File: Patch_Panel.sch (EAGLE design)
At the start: 24 parts

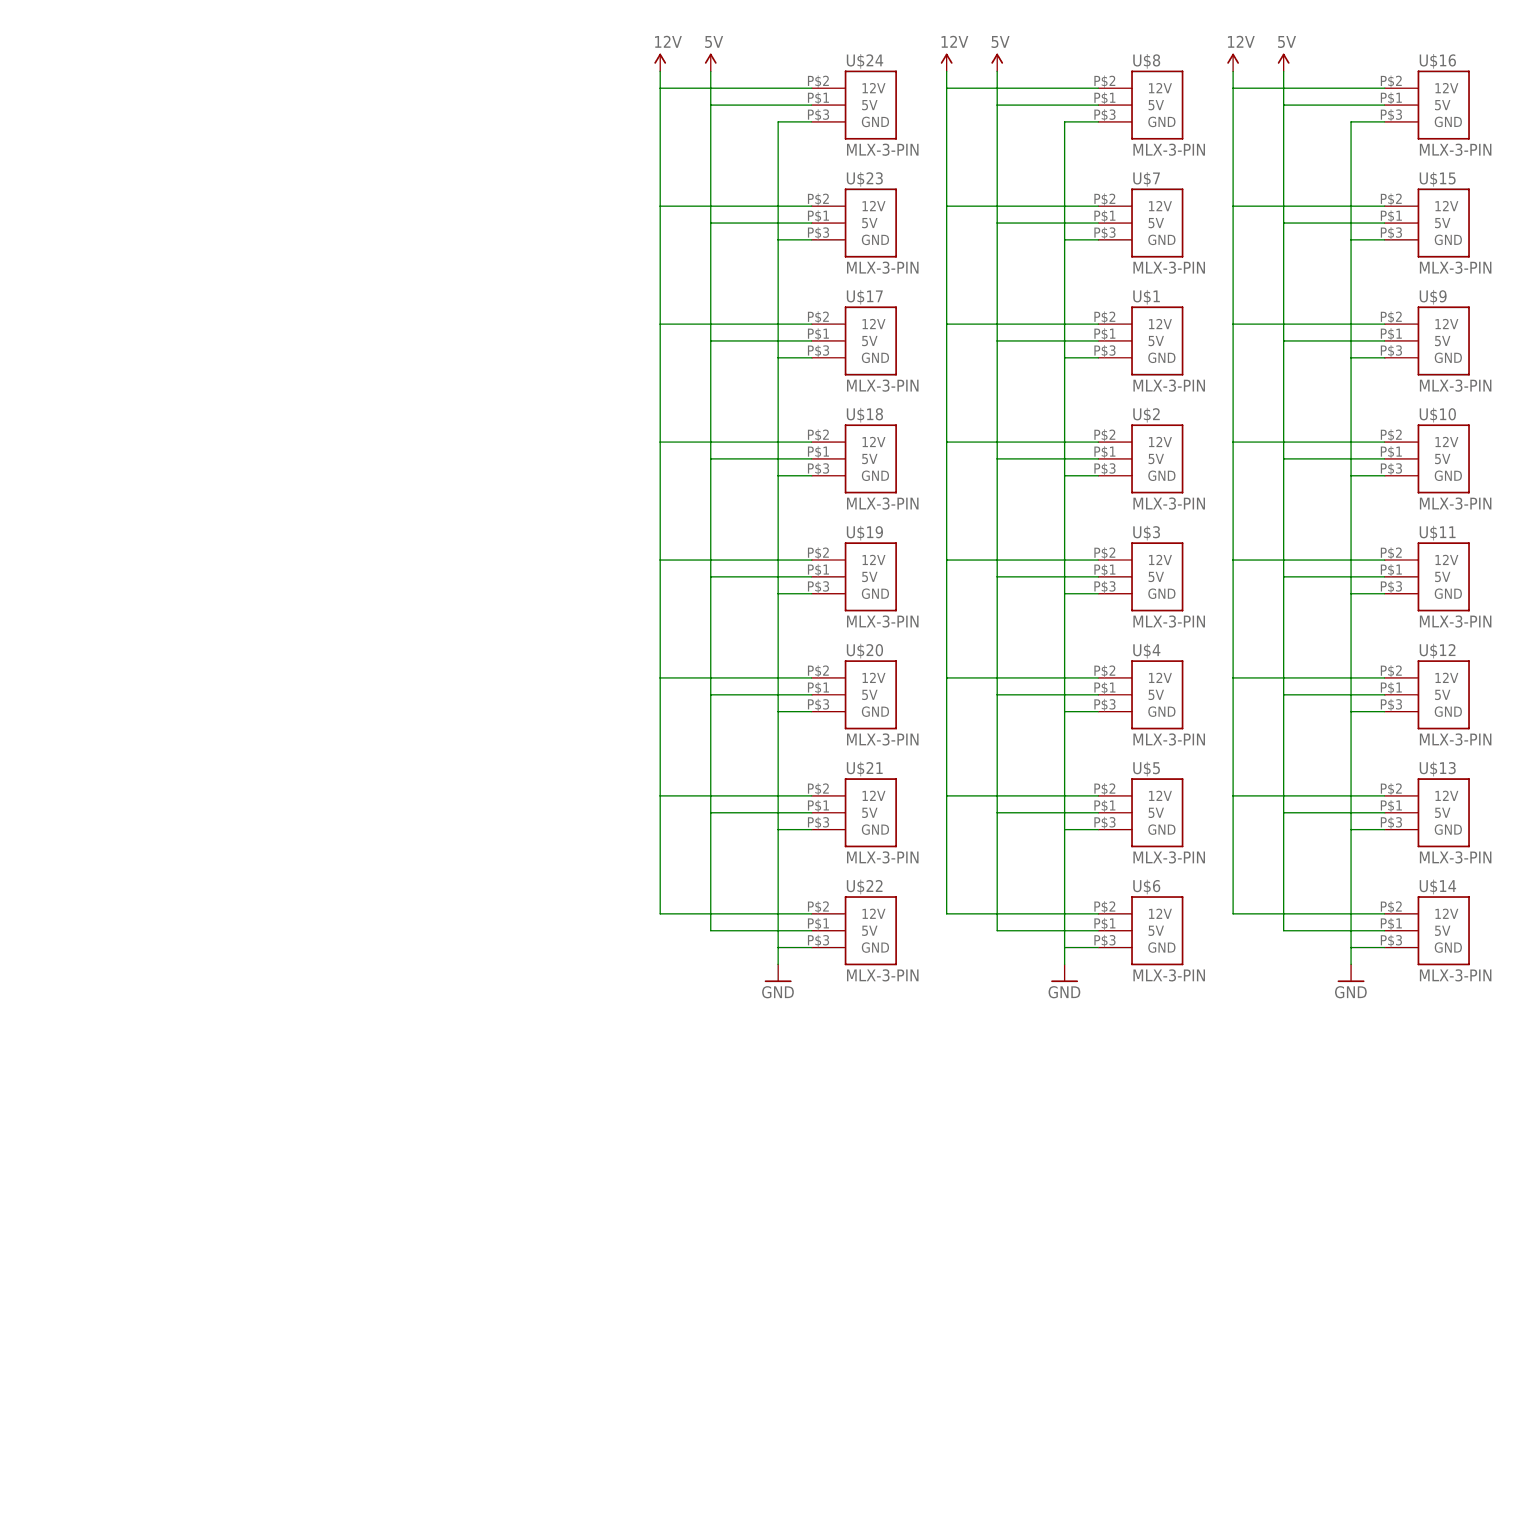
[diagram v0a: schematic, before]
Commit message: added moco power patch-thru, rearr 3-pin, gen dx
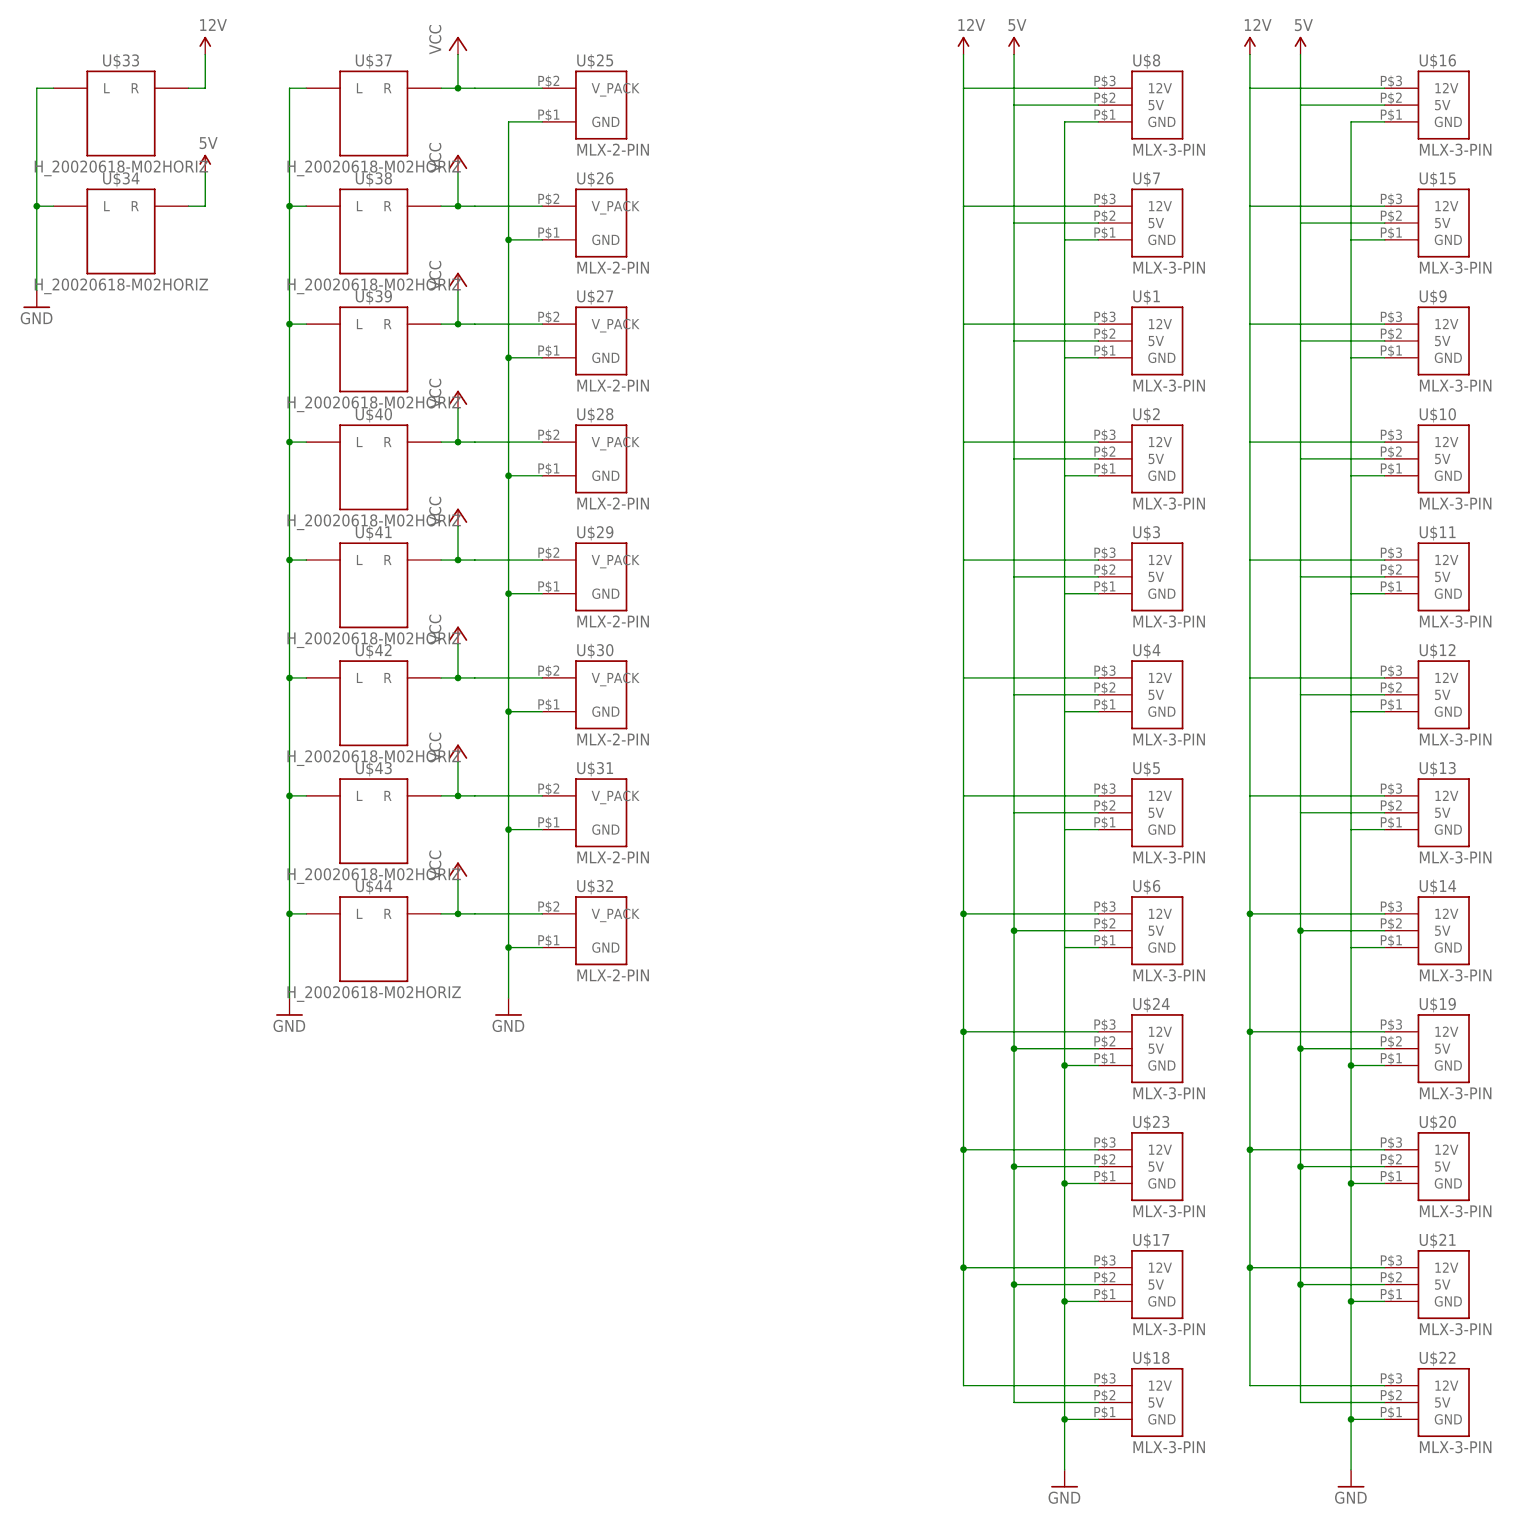
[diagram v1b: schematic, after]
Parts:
- added U$25, U$26, U$27, U$28, U$29, U$30, U$31, U$32: MLX-2-PIN, MRDT-2015-General:MLX-2-PIN
- added U$33, U$34, U$37, U$38, U$39, U$40, U$41, U$42, U$43, U$44: H_20020618-M02HORIZ, MRDT-2015-PowerBoard:H_20020618-M02HORIZ
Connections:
- new net MOCO_1: U$25.V_PACK, U$37.R
- new net MOCO_2: U$26.V_PACK, U$38.R
- new net MOCO_3: U$27.V_PACK, U$39.R
- new net MOCO_4: U$28.V_PACK, U$40.R
- new net MOCO_5: U$29.V_PACK, U$41.R
- new net MOCO_6: U$30.V_PACK, U$42.R
- new net MOCO_7: U$31.V_PACK, U$43.R
- new net MOCO_8: U$32.V_PACK, U$44.R
- net 12V: now also U$33.R
- net 5V: now also U$34.R
- net GND: now also U$25.GND, U$26.GND, U$27.GND, U$28.GND, U$29.GND, U$30.GND, U$31.GND, U$32.GND, U$33.L, U$34.L, U$37.L, U$38.L, U$39.L, U$40.L, U$41.L, U$42.L, U$43.L, U$44.L
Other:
- moved on the sheet: U$17, U$18, U$19, U$20, U$21, U$22, U$23, U$24

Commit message: Revert "added moco power patch-thru, rearr 3-pin, gen dx"
This reverts commit e393c53abb352ea2a1f007c95e73af8e49a976a5.
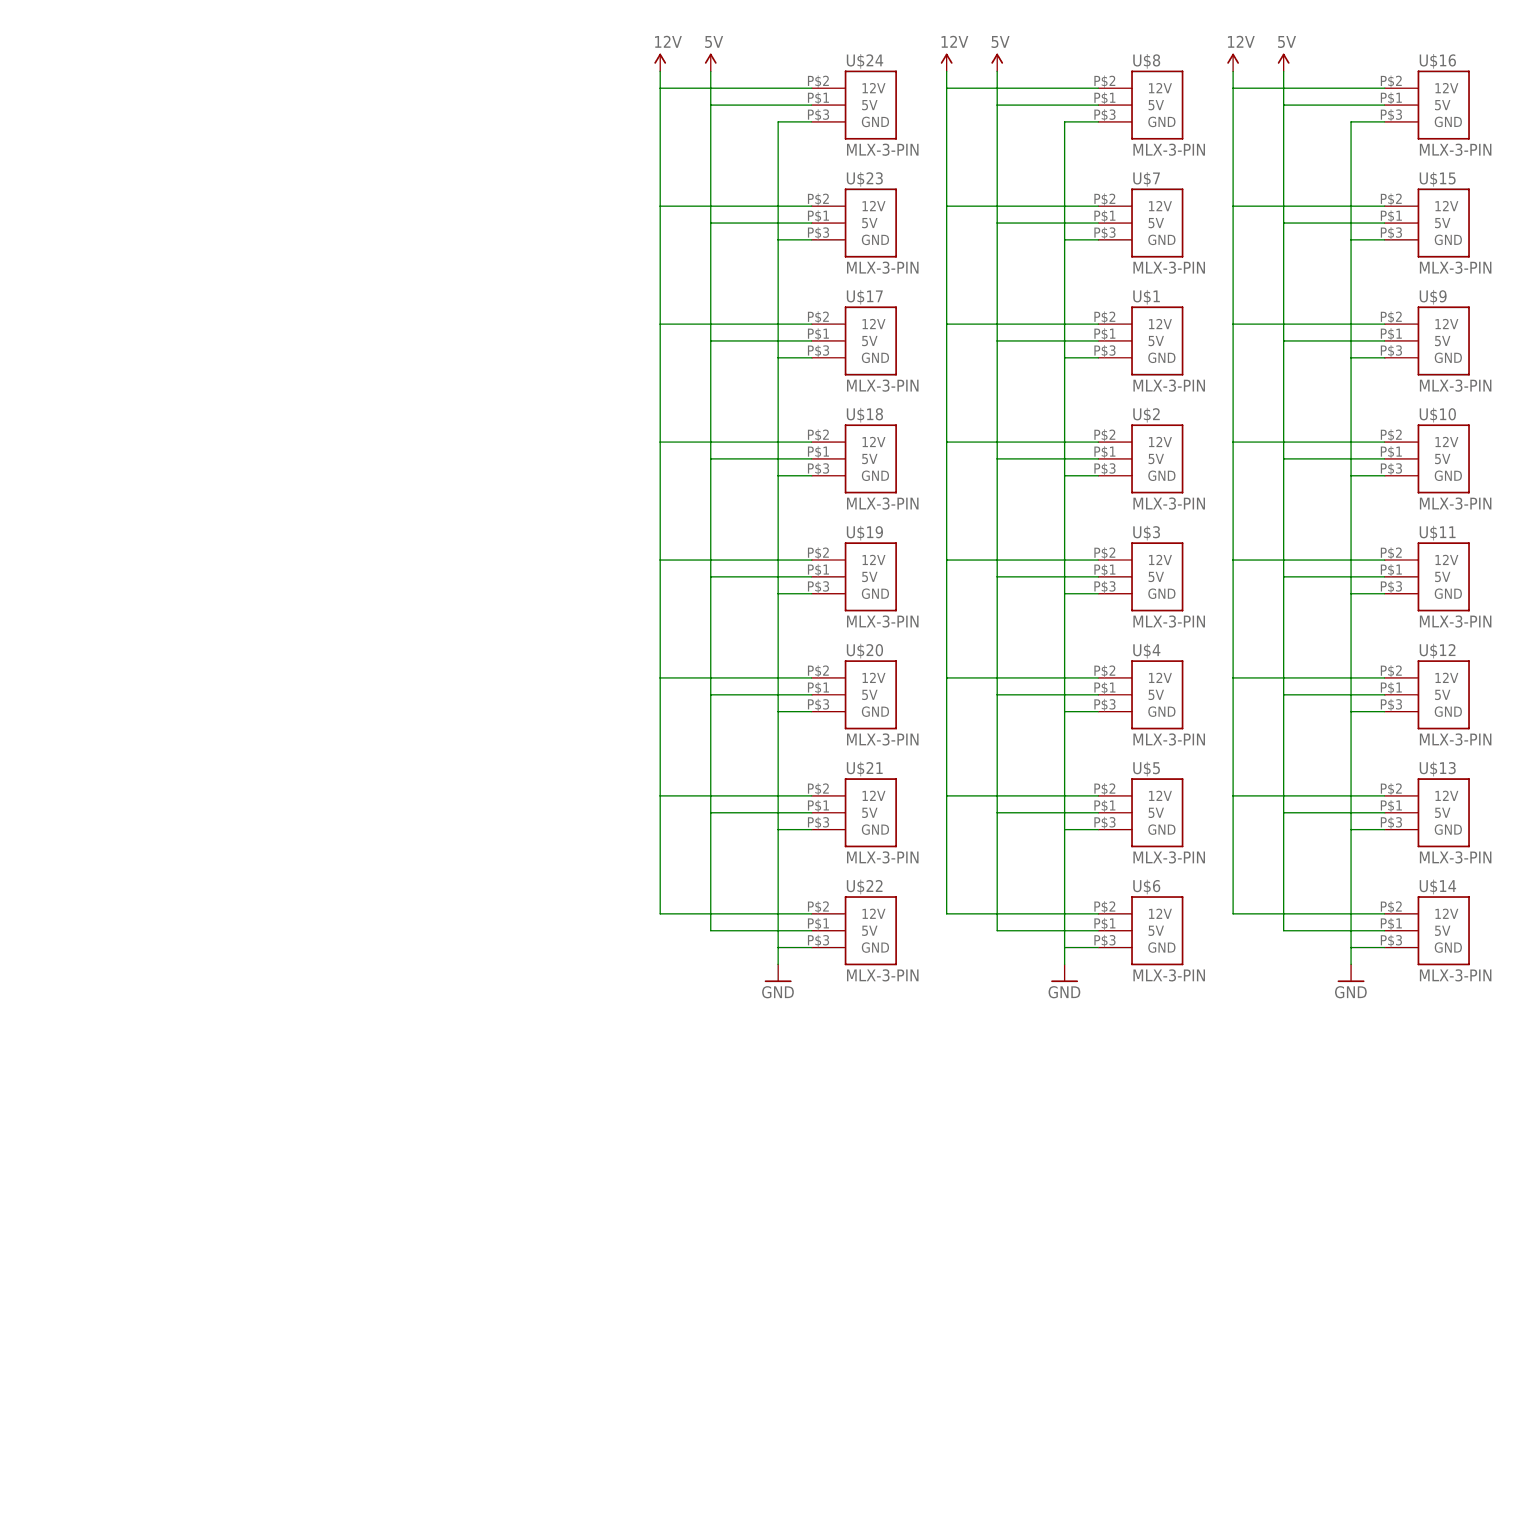
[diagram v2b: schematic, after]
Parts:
- removed U$25, U$26, U$27, U$28, U$29, U$30, U$31, U$32: MLX-2-PIN, MRDT-2015-General:MLX-2-PIN
- removed U$33, U$34, U$37, U$38, U$39, U$40, U$41, U$42, U$43, U$44: H_20020618-M02HORIZ, MRDT-2015-PowerBoard:H_20020618-M02HORIZ
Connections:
- removed net MOCO_1: U$25.V_PACK, U$37.R
- removed net MOCO_2: U$26.V_PACK, U$38.R
- removed net MOCO_3: U$27.V_PACK, U$39.R
- removed net MOCO_4: U$28.V_PACK, U$40.R
- removed net MOCO_5: U$29.V_PACK, U$41.R
- removed net MOCO_6: U$30.V_PACK, U$42.R
- removed net MOCO_7: U$31.V_PACK, U$43.R
- removed net MOCO_8: U$32.V_PACK, U$44.R
- net 12V: no longer U$33.R
- net 5V: no longer U$34.R
- net GND: no longer U$25.GND, U$26.GND, U$27.GND, U$28.GND, U$29.GND, U$30.GND, U$31.GND, U$32.GND, U$33.L, U$34.L, U$37.L, U$38.L, U$39.L, U$40.L, U$41.L, U$42.L, U$43.L, U$44.L
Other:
- moved on the sheet: U$17, U$18, U$19, U$20, U$21, U$22, U$23, U$24
